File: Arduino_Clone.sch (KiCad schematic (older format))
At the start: 0 parts

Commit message: Added new child sheet.
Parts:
- added BT?: Battery, symbol Device:Battery
- added C? (x2): C, symbol Device:C
- added C? (x2): CP, symbol Device:CP
- added D?: LED, symbol Device:LED
- added R? (x2): R, symbol Device:R
- added U?: 24LC1025, symbol Memory_EEPROM:24LC1025
- added U?: ATMEGA328P-AU, digikey-footprints:TQFP-32_7x7mm, symbol dk_Embedded-Microcontrollers:ATMEGA328P-AU
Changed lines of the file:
@@
 $Descr A4 11693 8268
 encoding utf-8
-Sheet 1 1
+Sheet 1 2
 Title "Arduino Clone"
 Date "2021-01-31"
@@
 Comment4 "Aurthor: Brycen Dhom"
 $EndDescr
+$Comp
+L Device:Battery BT?
+U 1 1 6016CB0C
+P 3625 2700
+F 0 "BT?" H 3733 2746 50  0000 L CNN
+F 1 "Battery" H 3733 2655 50  0000 L CNN
+F 2 "" V 3625 2760 50  0001 C CNN
+F 3 "~" V 3625 2760 50  0001 C CNN
+	1    3625 2700
+	1    0    0    -1
+$EndComp
+$Comp
+L Device:C C?
+U 1 1 6016DE4E
+P 3625 3275
+F 0 "C?" H 3740 3321 50  0000 L CNN
+F 1 "C" H 3740 3230 50  0000 L CNN
+F 2 "" H 3663 3125 50  0001 C CNN
+F 3 "~" H 3625 3275 50  0001 C CNN
+	1    3625 3275
+	1    0    0    -1
+$EndComp
+$Comp
+L Device:C C?
+U 1 1 6016E4DC
+P 3975 3275
+F 0 "C?" H 4090 3321 50  0000 L CNN
+F 1 "C" H 4090 3230 50  0000 L CNN
+F 2 "" H 4013 3125 50  0001 C CNN
+F 3 "~" H 3975 3275 50  0001 C CNN
+	1    3975 3275
+	1    0    0    -1
+$EndComp
+$Comp
+L Device:CP C?
+U 1 1 6016E8E4
+P 3625 3825
+F 0 "C?" H 3743 3871 50  0000 L CNN
+F 1 "CP" H 3743 3780 50  0000 L CNN
+F 2 "" H 3663 3675 50  0001 C CNN
+F 3 "~" H 3625 3825 50  0001 C CNN
+	1    3625 3825
+	1    0    0    -1
+$EndComp
+$Comp
+L Device:CP C?
+U 1 1 6016ED96
+P 3975 3825
+F 0 "C?" H 4093 3871 50  0000 L CNN
+F 1 "CP" H 4093 3780 50  0000 L CNN
+F 2 "" H 4013 3675 50  0001 C CNN
+F 3 "~" H 3975 3825 50  0001 C CNN
+	1    3975 3825
+	1    0    0    -1
+$EndComp
+$Comp
+L Device:LED D?
+U 1 1 6016F1E9
+P 3675 4275
+F 0 "D?" H 3668 4492 50  0000 C CNN
+F 1 "LED" H 3668 4401 50  0000 C CNN
+F 2 "" H 3675 4275 50  0001 C CNN
+F 3 "~" H 3675 4275 50  0001 C CNN
+	1    3675 4275
+	1    0    0    -1
+$EndComp
+$Comp
+L Device:R R?
+U 1 1 6016F7B9
+P 3675 4725
+F 0 "R?" H 3745 4771 50  0000 L CNN
+F 1 "R" H 3745 4680 50  0000 L CNN
+F 2 "" V 3605 4725 50  0001 C CNN
+F 3 "~" H 3675 4725 50  0001 C CNN
+	1    3675 4725
+	1    0    0    -1
+$EndComp
+$Comp
+L Device:R R?
+U 1 1 6016FC62
+P 4025 4725
+F 0 "R?" H 4095 4771 50  0000 L CNN
+F 1 "R" H 4095 4680 50  0000 L CNN
+F 2 "" V 3955 4725 50  0001 C CNN
+F 3 "~" H 4025 4725 50  0001 C CNN
+	1    4025 4725
+	1    0    0    -1
+$EndComp
+$Comp
+L Memory_EEPROM:24LC1025 U?
+U 1 1 60170312
+P 5300 3300
+F 0 "U?" H 5300 3781 50  0000 C CNN
+F 1 "24LC1025" H 5300 3690 50  0000 C CNN
+F 2 "" H 5300 3300 50  0001 C CNN
+F 3 "http://ww1.microchip.com/downloads/en/DeviceDoc/21941B.pdf" H 5300 3300 50  0001 C CNN
+	1    5300 3300
+	1    0    0    -1
+$EndComp
+$Comp
+L dk_Embedded-Microcontrollers:ATMEGA328P-AU U?
+U 1 1 601716D4
+P 7000 3200
+F 0 "U?" H 7328 3303 60  0000 L CNN
+F 1 "ATMEGA328P-AU" H 7328 3197 60  0000 L CNN
+F 2 "digikey-footprints:TQFP-32_7x7mm" H 7200 3400 60  0001 L CNN
+F 3 "http://www.microchip.com/mymicrochip/filehandler.aspx?ddocname=en608326" H 7200 3500 60  0001 L CNN
+F 4 "ATMEGA328P-AU-ND" H 7200 3600 60  0001 L CNN "Digi-Key_PN"
+F 5 "ATMEGA328P-AU" H 7200 3700 60  0001 L CNN "MPN"
+F 6 "Integrated Circuits (ICs)" H 7200 3800 60  0001 L CNN "Category"
+F 7 "Embedded - Microcontrollers" H 7200 3900 60  0001 L CNN "Family"
+F 8 "http://www.microchip.com/mymicrochip/filehandler.aspx?ddocname=en608326" H 7200 4000 60  0001 L CNN "DK_Datasheet_Link"
+F 9 "/product-detail/en/microchip-technology/ATMEGA328P-AU/ATMEGA328P-AU-ND/1832260" H 7200 4100 60  0001 L CNN "DK_Detail_Page"
+F 10 "IC MCU 8BIT 32KB FLASH 32TQFP" H 7200 4200 60  0001 L CNN "Description"
+F 11 "Microchip Technology" H 7200 4300 60  0001 L CNN "Manufacturer"
+F 12 "Active" H 7200 4400 60  0001 L CNN "Status"
+	1    7000 3200
+	1    0    0    -1
+$EndComp
+$Sheet
+S 5700 4850 5450 1600
+U 6017416D
+F0 "Connectors" 50
+F1 "Connectors.sch" 50
+$EndSheet
 $EndSCHEMATC

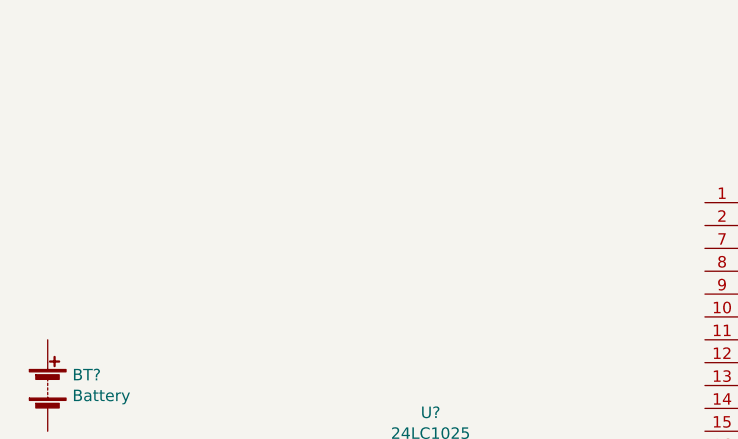
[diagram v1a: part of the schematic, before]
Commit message: Added custom clock IC symbol.
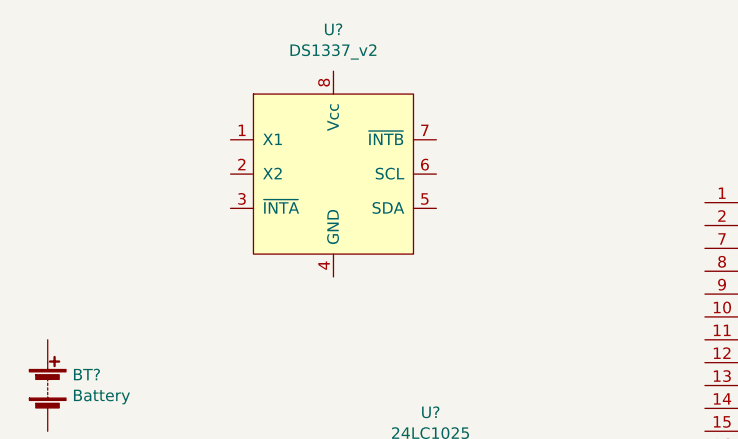
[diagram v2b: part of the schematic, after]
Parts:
- added U?: DS1337_v2, symbol My_Library:DS1337_v2
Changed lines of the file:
@@
 F1 "Connectors.sch" 50
 $EndSheet
+$Comp
+L My_Library:DS1337_v2 U?
+U 1 1 6017BB22
+P 4875 1775
+F 0 "U?" H 4875 2406 50  0000 C CNN
+F 1 "DS1337_v2" H 4875 2315 50  0000 C CNN
+F 2 "" H 4925 1825 50  0001 C CNN
+F 3 "https://datasheets.maximintegrated.com/en/ds/DS1337-DS1337C.pdf" H 4925 1825 50  0001 C CNN
+	1    4875 1775
+	1    0    0    -1
+$EndComp
 $EndSCHEMATC

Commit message: Added footprint associations.
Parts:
- removed C?: CP, symbol Device:CP
- added U2: 24LC1025, Footprints:SOIC-8_3.9mmX4.9mm, symbol Memory_EEPROM:24LC1025
- added Y1: Crystal 32 MHz, Crystal:Crystal_SMD_MicroCrystal_CC7V-T1A-2Pin_3.2x1.5mm_HandSoldering, symbol Device:Crystal
- added Y2: Crystal 60 MHz, Crystal:Crystal_SMD_5032-2Pin_5.0x3.2mm_HandSoldering, symbol Device:Crystal
- BT1: renamed from BT?; value Battery -> Battery 3V; footprint (none) -> Capacitor_SMD:C_0805_2012Metric
- C1, C2: renamed from C?; value C -> 22 pF; footprint (none) -> Capacitor_SMD:C_0805_2012Metric_Pad1.18x1.45mm_HandSolder
- C3: renamed from C?; value CP -> 10 uF; footprint (none) -> Capacitor_SMD:C_0805_2012Metric_Pad1.18x1.45mm_HandSolder
- D1: renamed from D?; footprint (none) -> LED_SMD:LED_0805_2012Metric_Pad1.15x1.40mm_HandSolder
- R1: renamed from R?; value R -> 330; footprint (none) -> Resistor_SMD:R_0805_2012Metric_Pad1.20x1.40mm_HandSolder
- R2: renamed from R?; value R -> 10k; footprint (none) -> Resistor_SMD:R_0805_2012Metric_Pad1.20x1.40mm_HandSolder
- U1: renamed from U?; footprint (none) -> Footprints:SOIC-8_3.9mmX4.9mm
- U3: renamed from U?; value DS1337_v2 -> DS1337+; footprint (none) -> Package_SO:SOIC-8_3.9x4.9mm_P1.27mm
- gave numbers to parts that had none: 1
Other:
- moved on the sheet: BT1, C1, C2, C3, D1, R1, R2, U1, U3, U4
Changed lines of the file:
@@
 $EndDescr
 $Comp
-L Device:Battery BT?
+L Device:Battery BT1
 U 1 1 6016CB0C
-P 3625 2700
-F 0 "BT?" H 3733 2746 50  0000 L CNN
-F 1 "Battery" H 3733 2655 50  0000 L CNN
-F 2 "" V 3625 2760 50  0001 C CNN
-F 3 "~" V 3625 2760 50  0001 C CNN
-	1    3625 2700
+P 9275 2050
+F 0 "BT1" H 9383 2096 50  0000 L CNN
+F 1 "Battery 3V" H 9383 2005 50  0000 L CNN
+F 2 "Capacitor_SMD:C_0805_2012Metric" V 9275 2110 50  0001 C CNN
+F 3 "~" V 9275 2110 50  0001 C CNN
+	1    9275 2050
 	1    0    0    -1
 $EndComp
 $Comp
-L Device:C C?
+L Device:C C1
 U 1 1 6016DE4E
-P 3625 3275
-F 0 "C?" H 3740 3321 50  0000 L CNN
-F 1 "C" H 3740 3230 50  0000 L CNN
-F 2 "" H 3663 3125 50  0001 C CNN
-F 3 "~" H 3625 3275 50  0001 C CNN
-	1    3625 3275
+P 5000 1950
+F 0 "C1" H 5115 1996 50  0000 L CNN
+F 1 "22 pF" H 5115 1905 50  0000 L CNN
+F 2 "Capacitor_SMD:C_0805_2012Metric_Pad1.18x1.45mm_HandSolder" H 5038 1800 50  0001 C CNN
+F 3 "~" H 5000 1950 50  0001 C CNN
+	1    5000 1950
 	1    0    0    -1
 $EndComp
 $Comp
-L Device:C C?
+L Device:C C2
 U 1 1 6016E4DC
-P 3975 3275
-F 0 "C?" H 4090 3321 50  0000 L CNN
-F 1 "C" H 4090 3230 50  0000 L CNN
-F 2 "" H 4013 3125 50  0001 C CNN
-F 3 "~" H 3975 3275 50  0001 C CNN
-	1    3975 3275
+P 5025 2525
+F 0 "C2" H 5140 2571 50  0000 L CNN
+F 1 "22 pF" H 5140 2480 50  0000 L CNN
+F 2 "Capacitor_SMD:C_0805_2012Metric_Pad1.18x1.45mm_HandSolder" H 5063 2375 50  0001 C CNN
+F 3 "~" H 5025 2525 50  0001 C CNN
+	1    5025 2525
 	1    0    0    -1
 $EndComp
 $Comp
-L Device:CP C?
+L Device:CP C3
 U 1 1 6016E8E4
-P 3625 3825
-F 0 "C?" H 3743 3871 50  0000 L CNN
-F 1 "CP" H 3743 3780 50  0000 L CNN
-F 2 "" H 3663 3675 50  0001 C CNN
-F 3 "~" H 3625 3825 50  0001 C CNN
-	1    3625 3825
+P 9275 3175
+F 0 "C3" H 9393 3221 50  0000 L CNN
+F 1 "10 uF" H 9393 3130 50  0000 L CNN
+F 2 "Capacitor_SMD:C_0805_2012Metric_Pad1.18x1.45mm_HandSolder" H 9313 3025 50  0001 C CNN
+F 3 "~" H 9275 3175 50  0001 C CNN
+	1    9275 3175
 	1    0    0    -1
 $EndComp
 $Comp
-L Device:CP C?
-U 1 1 6016ED96
-P 3975 3825
-F 0 "C?" H 4093 3871 50  0000 L CNN
-F 1 "CP" H 4093 3780 50  0000 L CNN
-F 2 "" H 4013 3675 50  0001 C CNN
-F 3 "~" H 3975 3825 50  0001 C CNN
-	1    3975 3825
+L Device:LED D1
+U 1 1 6016F1E9
+P 4950 3125
+F 0 "D1" H 4943 3342 50  0000 C CNN
+F 1 "LED" H 4943 3251 50  0000 C CNN
+F 2 "LED_SMD:LED_0805_2012Metric_Pad1.15x1.40mm_HandSolder" H 4950 3125 50  0001 C CNN
+F 3 "~" H 4950 3125 50  0001 C CNN
+	1    4950 3125
 	1    0    0    -1
 $EndComp
 $Comp
-L Device:LED D?
-U 1 1 6016F1E9
-P 3675 4275
-F 0 "D?" H 3668 4492 50  0000 C CNN
-F 1 "LED" H 3668 4401 50  0000 C CNN
-F 2 "" H 3675 4275 50  0001 C CNN
-F 3 "~" H 3675 4275 50  0001 C CNN
-	1    3675 4275
+L Device:R R1
+U 1 1 6016F7B9
+P 5025 3825
+F 0 "R1" H 5095 3871 50  0000 L CNN
+F 1 "330" H 5095 3780 50  0000 L CNN
+F 2 "Resistor_SMD:R_0805_2012Metric_Pad1.20x1.40mm_HandSolder" V 4955 3825 50  0001 C CNN
+F 3 "~" H 5025 3825 50  0001 C CNN
+	1    5025 3825
 	1    0    0    -1
 $EndComp
 $Comp
-L Device:R R?
-U 1 1 6016F7B9
-P 3675 4725
-F 0 "R?" H 3745 4771 50  0000 L CNN
-F 1 "R" H 3745 4680 50  0000 L CNN
-F 2 "" V 3605 4725 50  0001 C CNN
-F 3 "~" H 3675 4725 50  0001 C CNN
-	1    3675 4725
+L Device:R R2
+U 1 1 6016FC62
+P 5375 3825
+F 0 "R2" H 5445 3871 50  0000 L CNN
+F 1 "10k" H 5445 3780 50  0000 L CNN
+F 2 "Resistor_SMD:R_0805_2012Metric_Pad1.20x1.40mm_HandSolder" V 5305 3825 50  0001 C CNN
+F 3 "~" H 5375 3825 50  0001 C CNN
+	1    5375 3825
 	1    0    0    -1
 $EndComp
 $Comp
-L Device:R R?
-U 1 1 6016FC62
-P 4025 4725
-F 0 "R?" H 4095 4771 50  0000 L CNN
-F 1 "R" H 4095 4680 50  0000 L CNN
-F 2 "" V 3955 4725 50  0001 C CNN
-F 3 "~" H 4025 4725 50  0001 C CNN
-	1    4025 4725
+L Memory_EEPROM:24LC1025 U1
+U 1 1 60170312
+P 2175 5300
+F 0 "U1" H 2175 5781 50  0000 C CNN
+F 1 "24LC1025" H 2175 5690 50  0000 C CNN
+F 2 "Footprints:SOIC-8_3.9mmX4.9mm" H 2175 5300 50  0001 C CNN
+F 3 "http://ww1.microchip.com/downloads/en/DeviceDoc/21941B.pdf" H 2175 5300 50  0001 C CNN
+	1    2175 5300
 	1    0    0    -1
 $EndComp
 $Comp
-L Memory_EEPROM:24LC1025 U?
-U 1 1 60170312
-P 5300 3300
-F 0 "U?" H 5300 3781 50  0000 C CNN
-F 1 "24LC1025" H 5300 3690 50  0000 C CNN
-F 2 "" H 5300 3300 50  0001 C CNN
-F 3 "http://ww1.microchip.com/downloads/en/DeviceDoc/21941B.pdf" H 5300 3300 50  0001 C CNN
-	1    5300 3300
-	1    0    0    -1
-$EndComp
-$Comp
-L dk_Embedded-Microcontrollers:ATMEGA328P-AU U?
+L dk_Embedded-Microcontrollers:ATMEGA328P-AU U4
 U 1 1 601716D4
-P 7000 3200
-F 0 "U?" H 7328 3303 60  0000 L CNN
-F 1 "ATMEGA328P-AU" H 7328 3197 60  0000 L CNN
-F 2 "digikey-footprints:TQFP-32_7x7mm" H 7200 3400 60  0001 L CNN
-F 3 "http://www.microchip.com/mymicrochip/filehandler.aspx?ddocname=en608326" H 7200 3500 60  0001 L CNN
-F 4 "ATMEGA328P-AU-ND" H 7200 3600 60  0001 L CNN "Digi-Key_PN"
-F 5 "ATMEGA328P-AU" H 7200 3700 60  0001 L CNN "MPN"
-F 6 "Integrated Circuits (ICs)" H 7200 3800 60  0001 L CNN "Category"
-F 7 "Embedded - Microcontrollers" H 7200 3900 60  0001 L CNN "Family"
-F 8 "http://www.microchip.com/mymicrochip/filehandler.aspx?ddocname=en608326" H 7200 4000 60  0001 L CNN "DK_Datasheet_Link"
-F 9 "/product-detail/en/microchip-technology/ATMEGA328P-AU/ATMEGA328P-AU-ND/1832260" H 7200 4100 60  0001 L CNN "DK_Detail_Page"
-F 10 "IC MCU 8BIT 32KB FLASH 32TQFP" H 7200 4200 60  0001 L CNN "Description"
-F 11 "Microchip Technology" H 7200 4300 60  0001 L CNN "Manufacturer"
-F 12 "Active" H 7200 4400 60  0001 L CNN "Status"
-	1    7000 3200
+P 6375 2925
+F 0 "U4" H 6703 3028 60  0000 L CNN
+F 1 "ATMEGA328P-AU" H 6703 2922 60  0000 L CNN
+F 2 "digikey-footprints:TQFP-32_7x7mm" H 6575 3125 60  0001 L CNN
+F 3 "http://www.microchip.com/mymicrochip/filehandler.aspx?ddocname=en608326" H 6575 3225 60  0001 L CNN
+F 4 "ATMEGA328P-AU-ND" H 6575 3325 60  0001 L CNN "Digi-Key_PN"
+F 5 "ATMEGA328P-AU" H 6575 3425 60  0001 L CNN "MPN"
+F 6 "Integrated Circuits (ICs)" H 6575 3525 60  0001 L CNN "Category"
+F 7 "Embedded - Microcontrollers" H 6575 3625 60  0001 L CNN "Family"
+F 8 "http://www.microchip.com/mymicrochip/filehandler.aspx?ddocname=en608326" H 6575 3725 60  0001 L CNN "DK_Datasheet_Link"
+F 9 "/product-detail/en/microchip-technology/ATMEGA328P-AU/ATMEGA328P-AU-ND/1832260" H 6575 3825 60  0001 L CNN "DK_Detail_Page"
+F 10 "IC MCU 8BIT 32KB FLASH 32TQFP" H 6575 3925 60  0001 L CNN "Description"
+F 11 "Microchip Technology" H 6575 4025 60  0001 L CNN "Manufacturer"
+F 12 "Active" H 6575 4125 60  0001 L CNN "Status"
+	1    6375 2925
 	1    0    0    -1
 $EndComp
 $Sheet
-S 5700 4850 5450 1600
+S 875  6025 5450 1600
 U 6017416D
 F0 "Connectors" 50
@@
 $EndSheet
 $Comp
-L My_Library:DS1337_v2 U?
+L My_Library:DS1337_v2 U3
 U 1 1 6017BB22
-P 4875 1775
-F 0 "U?" H 4875 2406 50  0000 C CNN
-F 1 "DS1337_v2" H 4875 2315 50  0000 C CNN
-F 2 "" H 4925 1825 50  0001 C CNN
-F 3 "https://datasheets.maximintegrated.com/en/ds/DS1337-DS1337C.pdf" H 4925 1825 50  0001 C CNN
-	1    4875 1775
+P 2400 1325
+F 0 "U3" H 2400 1956 50  0000 C CNN
+F 1 "DS1337+" H 2400 1865 50  0000 C CNN
+F 2 "Package_SO:SOIC-8_3.9x4.9mm_P1.27mm" H 2450 1375 50  0001 C CNN
+F 3 "https://datasheets.maximintegrated.com/en/ds/DS1337-DS1337C.pdf" H 2450 1375 50  0001 C CNN
+	1    2400 1325
 	1    0    0    -1
 $EndComp
+$Comp
+L Device:Crystal Y1
+U 1 1 6017D062
+P 1550 1175
+F 0 "Y1" H 1550 1443 50  0000 C CNN
+F 1 "Crystal 32 MHz" H 1550 1352 50  0000 C CNN
+F 2 "Crystal:Crystal_SMD_MicroCrystal_CC7V-T1A-2Pin_3.2x1.5mm_HandSoldering" H 1550 1175 50  0001 C CNN
+F 3 "~" H 1550 1175 50  0001 C CNN
+	1    1550 1175
+	1    0    0    -1
+$EndComp
+$Comp
+L Device:Crystal Y2
+U 1 1 6017DF24
+P 5350 2150
+F 0 "Y2" H 5350 2418 50  0000 C CNN
+F 1 "Crystal 60 MHz" H 5350 2327 50  0000 C CNN
+F 2 "Crystal:Crystal_SMD_5032-2Pin_5.0x3.2mm_HandSoldering" H 5350 2150 50  0001 C CNN
+F 3 "~" H 5350 2150 50  0001 C CNN
+	1    5350 2150
+	1    0    0    -1
+$EndComp
+$Comp
+L Memory_EEPROM:24LC1025 U2
+U 1 1 6018204D
+P 2225 4175
+F 0 "U2" H 2225 4656 50  0000 C CNN
+F 1 "24LC1025" H 2225 4565 50  0000 C CNN
+F 2 "Footprints:SOIC-8_3.9mmX4.9mm" H 2225 4175 50  0001 C CNN
+F 3 "http://ww1.microchip.com/downloads/en/DeviceDoc/21941B.pdf" H 2225 4175 50  0001 C CNN
+	1    2225 4175
+	1    0    0    -1
+$EndComp
